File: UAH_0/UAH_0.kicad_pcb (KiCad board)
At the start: 2 copper layers, 190 x 100 mm, 118 parts, among them X10 Check_point, X11 Check_point, X12 Check_point, X13 Check_point, X17 Check_point, X18 Check_point, X2 Check_point, X3 Крепежное_отверстие_М3, X4 Крепежное_отверстие_М3, X5 Крепежное_отверстие_М3, X6 Крепежное_отверстие_М3, X7 LOGO_NIKITOS_19х7, X8 Check_point, X9 Check_point

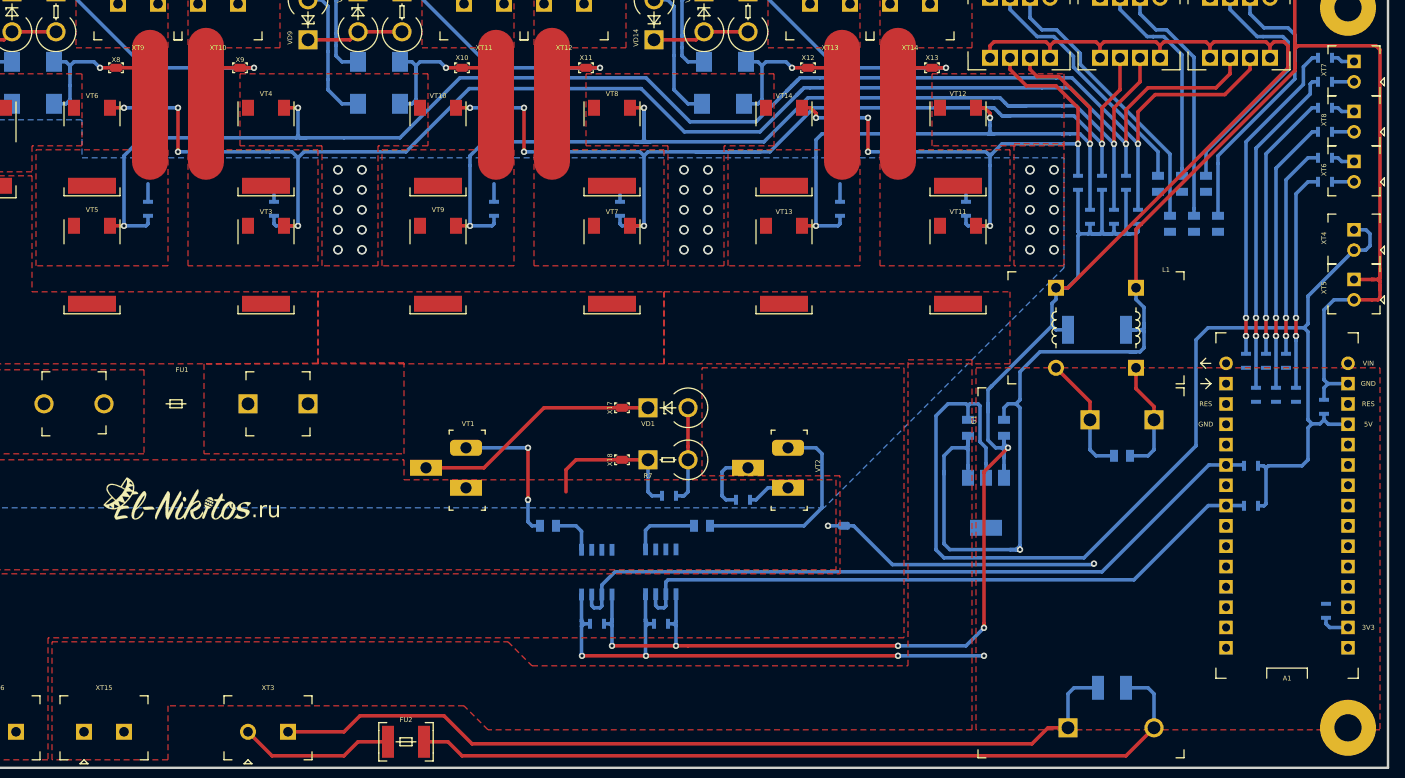
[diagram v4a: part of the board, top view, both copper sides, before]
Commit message: закончена трассировка, надо добавить лого и маркировка, PDF обновлен
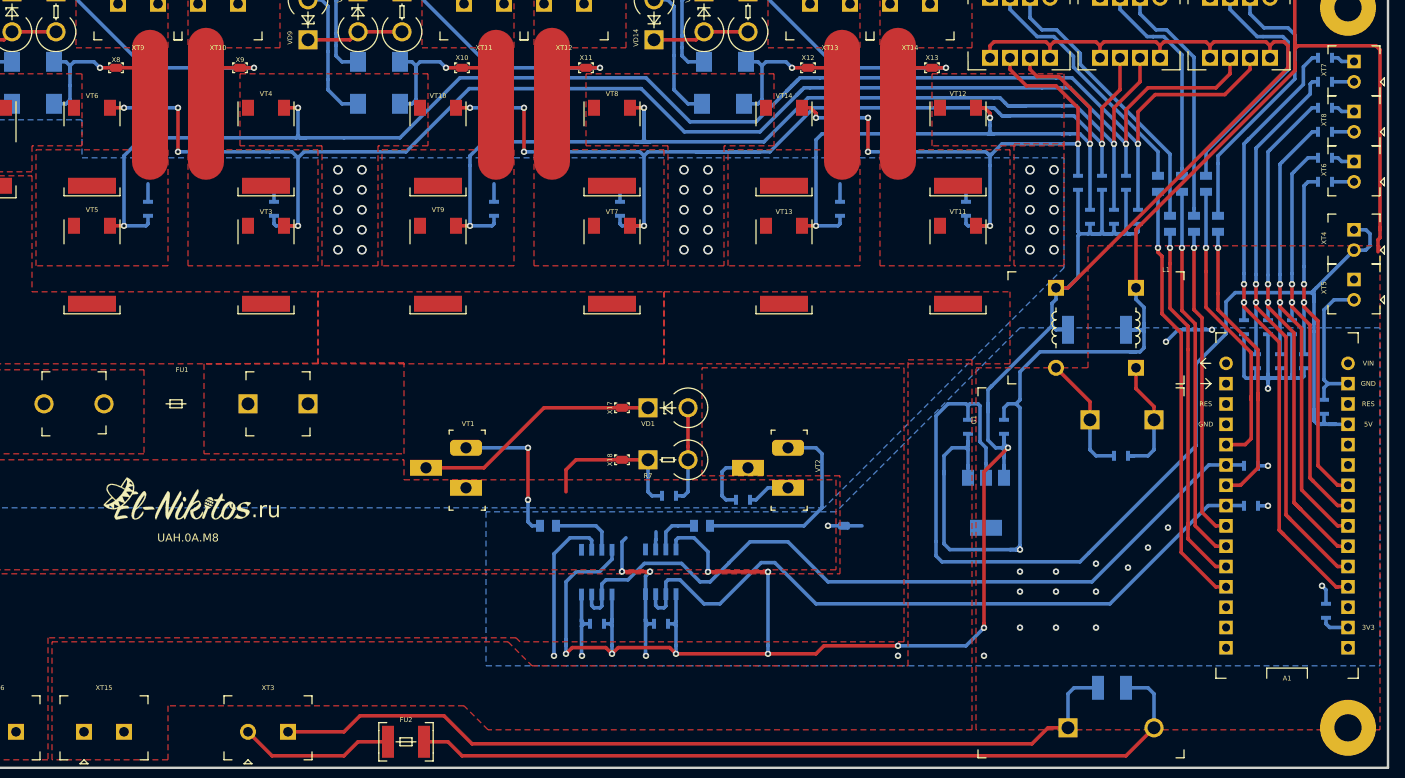
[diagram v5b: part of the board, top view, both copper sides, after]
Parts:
- C13, C15, C8: footprint MOTOR_RLC:Конденсатор_SMD_0805 -> MOTOR_RLC:Конденсатор_SMD_К10-83(0603)
- moved C4 4.32 mm to (229.5, 98.3)
- moved C1 4.27 mm to (228.0, 94.0)
- moved C6 4.23 mm to (226.5, 98.3)
- moved C2 4.21 mm to (222.0, 94.0)
- moved C3 4.21 mm to (225.0, 94.0)
- moved C5 4.20 mm to (223.5, 98.3)
- moved C13 0.25 mm to (192.0, 108.2)
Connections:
- A1 pad 10: Net-(A1-Pad10) -> /MC_DIN_6
- A1 pad 11: Net-(A1-Pad11) -> /MC_DIN_3
- A1 pad 12: Net-(A1-Pad12) -> /MC_DIN_4
- A1 pad 20: /MC_DIN_6 -> /MOTOR_1_SPIN_1
- A1 pad 22: /MC_DIN_5 -> /MOTOR_1_SPIN_2
- A1 pad 24: /MC_DIN_4 -> /MOTOR_2_SPIN_2
- A1 pad 25: /MC_DIN_3 -> /MOTOR_2_SPIN_1
- A1 pad 26: /MC_DIN_2 -> /MOTOR_3_SPIN_2
- A1 pad 27: /MC_DIN_1 -> /MOTOR_3_SPIN_1
- A1 pad 7: Net-(A1-Pad7) -> /MC_DIN_1
- A1 pad 8: Net-(A1-Pad8) -> /MC_DIN_2
- A1 pad 9: Net-(A1-Pad9) -> /MC_DIN_5
- DD1 pad 5: /DRIVE_1 -> Net-(DD1-Pad5)
- DD1 pad 6: Net-(DD1-Pad6) -> /0(12V)_MC
- DD1 pad 7: Net-(DD1-Pad7) -> /DRIVE_1
- DD1 pad 8: Net-(DD1-Pad8) -> /15V_MOSFET
- DD2 pad 5: /DRIVE_2 -> Net-(DD2-Pad5)
- DD2 pad 6: Net-(DD2-Pad6) -> /0(12V)_MC
- DD2 pad 7: Net-(DD2-Pad7) -> /DRIVE_2
- DD2 pad 8: Net-(DD2-Pad8) -> /15V_MOSFET
- R10 pad 1: /PWR_COMMUTATION_1/MODE_1 -> /MOTOR_1_SPIN_1
- R11 pad 1: /PWR_COMMUTATION_1/MODE_2 -> /MOTOR_1_SPIN_2
- R13 pad 1: /PWR_COMMUTATION_2/MODE_1 -> /MOTOR_2_SPIN_1
- R14 pad 1: /PWR_COMMUTATION_2/MODE_2 -> /MOTOR_2_SPIN_2
- R16 pad 1: /sheet5F495C51/MODE_1 -> /MOTOR_3_SPIN_1
- R17 pad 1: /sheet5F495C51/MODE_2 -> /MOTOR_3_SPIN_2
- R8 pad 2: /5V_MC -> /0(12V)_MC
- R9 pad 2: /5V_MC -> /0(12V)_MC
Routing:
- net /15V_MOSFET: track 259.3 -> 313.6 mm, vias 5 -> 9
- net /MOTOR_3_SPIN_1: track 0.00 -> 53.7 mm, vias 0 -> 1
- net /MOTOR_2_SPIN_1: track 0.00 -> 47.3 mm, vias 0 -> 1
- net /MOTOR_3_SPIN_2: track 0.00 -> 46.0 mm, vias 0 -> 1
- net /MOTOR_2_SPIN_2: track 0.00 -> 39.2 mm, vias 0 -> 1
- net /MC_DIN_4: track 41.1 -> 79.9 mm
- net /MOTOR_1_SPIN_2: track 0.00 -> 37.2 mm, vias 0 -> 1
- net /MOTOR_1_SPIN_1: track 0.00 -> 37.0 mm, vias 0 -> 1
- net /MC_DIN_3: track 41.9 -> 76.8 mm
- net /MC_DIN_6: track 33.9 -> 66.0 mm
- net /MC_DIN_5: track 34.6 -> 62.4 mm
- net /MC_DIN_2: track 26.9 -> 51.7 mm
- net /MC_DIN_1: track 27.6 -> 48.9 mm
- net /0(12V)_MC: track 356.1 -> 341.9 mm, vias 6 -> 26
- net /5V_MC: track 153.7 -> 145.1 mm
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- added copper zone on B.Cu, net /0(12V)_MC
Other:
- board text added: "UAH.0A.M8"

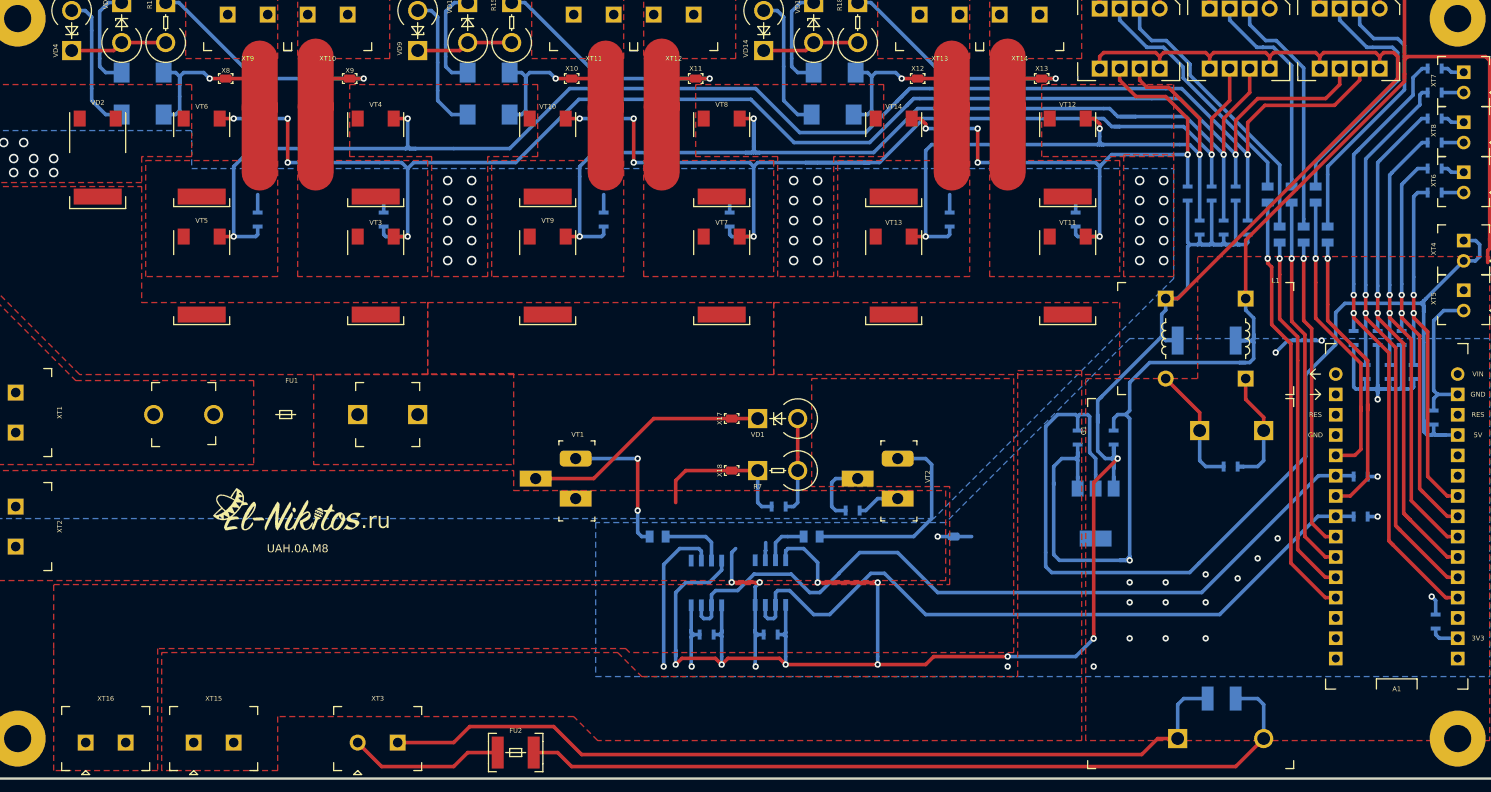
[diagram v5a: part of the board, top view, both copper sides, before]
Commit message: добавлена маркировка, обновлены STEP, PDF, PNG, нет ЛОГО заказчика
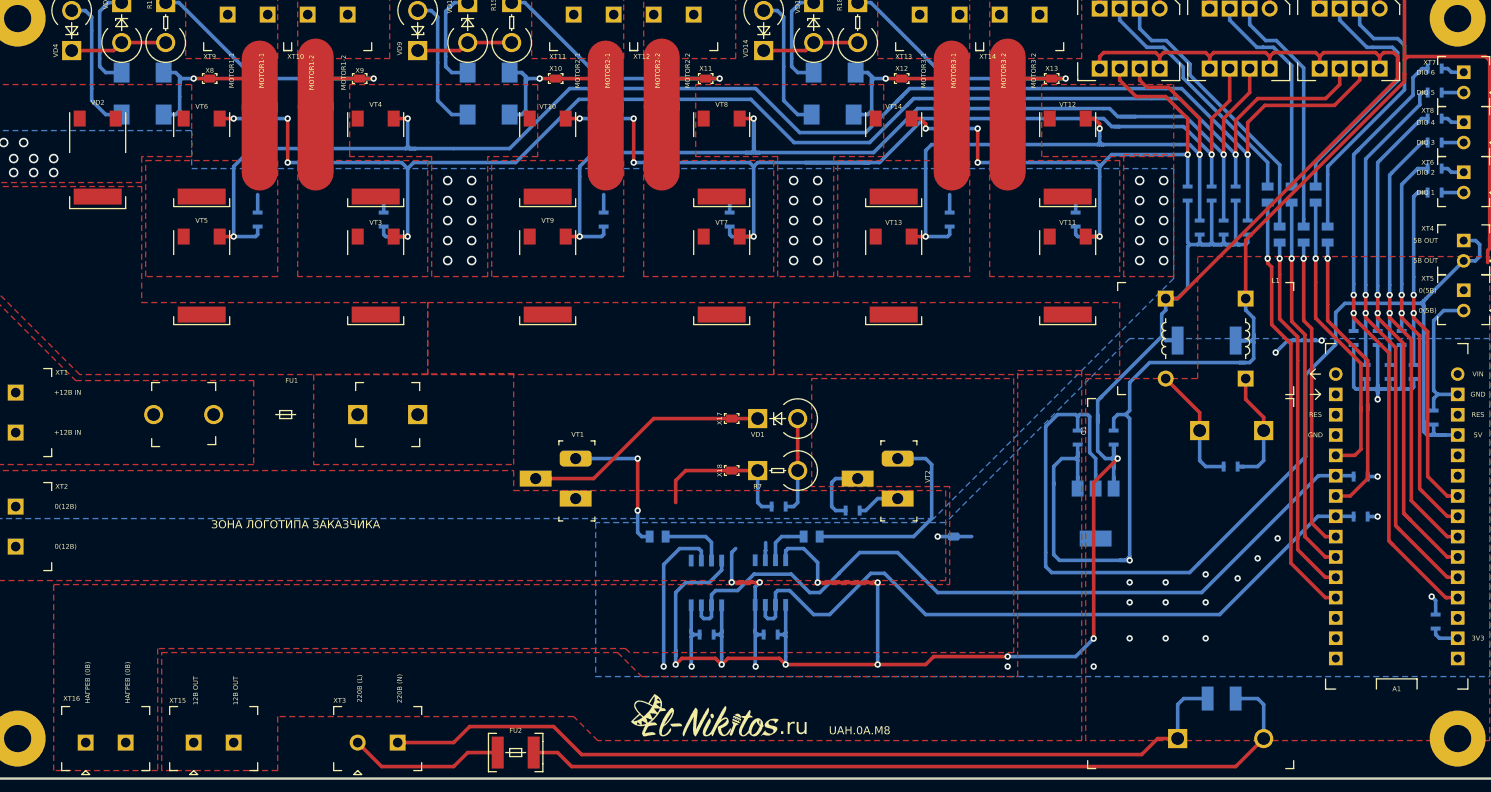
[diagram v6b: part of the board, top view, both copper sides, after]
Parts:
- moved X7 58.3 mm to (141.2, 142.5)
- moved X10 2.00 mm to (122.2, 62.5)
- moved X12 2.00 mm to (165.5, 62.5)
- moved X8 2.00 mm to (79.0, 62.5)
- moved X11 1.25 mm to (141.0, 62.5)
- moved X13 1.25 mm to (184.2, 62.5)
- moved X9 1.25 mm to (97.8, 62.5)
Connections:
- A1 pad 10: /MC_DIN_6 -> /MC_DIN_4
- A1 pad 11: /MC_DIN_3 -> /MC_DIN_5
- A1 pad 12: /MC_DIN_4 -> /MC_DIN_6
- A1 pad 9: /MC_DIN_5 -> /MC_DIN_3
- C2 pad 1: /MC_DIN_4 -> /MC_DIN_6
- C3 pad 1: /MC_DIN_6 -> /MC_DIN_4
- C5 pad 1: /MC_DIN_3 -> /MC_DIN_5
- C6 pad 1: /MC_DIN_5 -> /MC_DIN_3
- R3 pad 1: /D_IN_3 -> /D_IN_5
- R3 pad 2: /MC_DIN_3 -> /MC_DIN_5
- R4 pad 1: /D_IN_4 -> /D_IN_6
- R4 pad 2: /MC_DIN_4 -> /MC_DIN_6
- R5 pad 1: /D_IN_5 -> /D_IN_3
- R5 pad 2: /MC_DIN_5 -> /MC_DIN_3
- R6 pad 1: /D_IN_6 -> /D_IN_4
- R6 pad 2: /MC_DIN_6 -> /MC_DIN_4
- XT7 pad 1: /D_IN_3 -> /D_IN_5
- XT7 pad 2: /D_IN_4 -> /D_IN_6
- XT8 pad 1: /D_IN_5 -> /D_IN_3
- XT8 pad 2: /D_IN_6 -> /D_IN_4
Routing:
- net /MC_DIN_5: track 62.4 -> 76.8 mm
- net /MC_DIN_3: track 76.8 -> 62.4 mm
- net /MC_DIN_6: track 66.0 -> 79.9 mm
- net /MC_DIN_4: track 79.9 -> 66.0 mm
- net /OUT_3_1: track 31.2 -> 34.5 mm
- net /OUT_2_1: track 31.2 -> 34.5 mm
- net /OUT_1_1: track 31.2 -> 34.5 mm
- net /OUT_3_2: track 17.2 -> 18.9 mm
- net /OUT_2_2: track 17.2 -> 18.9 mm
- net /OUT_1_2: track 17.2 -> 18.9 mm
- net Net-(VD3-Pad2): track 15.2 -> 13.6 mm
- net Net-(R18-Pad2): track 29.9 -> 31.2 mm
- net Net-(R15-Pad2): track 29.9 -> 31.2 mm
- net Net-(R12-Pad2): track 29.9 -> 31.2 mm
- net Net-(VD13-Pad2): track 14.4 -> 15.3 mm
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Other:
- board text added: "+12В IN"
- board text added: "0(12В)"
- board text added: "0(5В)"
- board text added: "12В OUT"
- board text added: "220В (L)"
- board text added: "220В (N)"
- board text added: "5В OUT"
- board text added: "DIO 1"
- board text added: "DIO 2"
- board text added: "DIO 3"
- board text added: "DIO 4"
- board text added: "DIO 5"
- board text added: "DIO 6"
- board text added: "MOTOR1-1"
- board text added: "MOTOR1-2"
- board text added: "MOTOR2-1"
- board text added: "MOTOR2-2"
- board text added: "MOTOR3-1"
- board text added: "MOTOR3-2"
- board text added: "ЗОНА ЛОГОТИПА ЗАКАЗЧИКА"
- board text added: "НАГРЕВ (0В)"

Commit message: UAH_0B, готова плата +gerbers
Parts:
- added X1: LOGO_NIKITOS_19х7, N_ICO:trinity_32x10, F.Cu at (92.2, 118.2)
- added X14: LOGO_NIKITOS_19х7, N_ICO:El-nikitos_QR_10x10, B.Cu at (118.0, 126.8)
- X7: footprint N_ICO:el-nikitos_19x7 -> N_ICO:ni_10x10; moved to B.Cu
- moved X7 38.2 mm to (106.2, 127.2), turned to 180 degrees
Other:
- board text added: "0V"
- board text added: "COM"
- board text added: "OUT11"
- board text added: "OUT12"
- board text added: "OUT21"
- board text added: "OUT22"
- board text added: "OUT31"
- board text added: "OUT32"
- board text added: "UAH.0B.M8"
- board text removed: ".ru"
- board text removed: "UAH.0A.M8"
- board text removed: "ЗОНА ЛОГОТИПА ЗАКАЗЧИКА"
